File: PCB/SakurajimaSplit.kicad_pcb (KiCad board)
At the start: 2 copper layers, 302 x 112.4 mm, 180 parts, among them J1 SWD, J2 USB-C to Right-Half, J3 VREF+, J4 SWD, J5 USB-C to Host, J6 VREF+, J7 USB-C to Right-Half, SW1 SWCLK/BOOT0, SW2 SWCLK/BOOT0, U1 USBLC6-2SC6, U10 ZJY_M233, U11 ZJY_M233, U2 STM32G0B1CBT6, U3 W25Q128JVS, U4 TLV76733DRVR, U5 USBLC6-2SC6, U6 STM32G0B1CBT6, U7 W25Q128JVS, U8 TLV76733DRVR, U9 USBLC6-2SC6, Y1 8MHz, Y2 8MHz

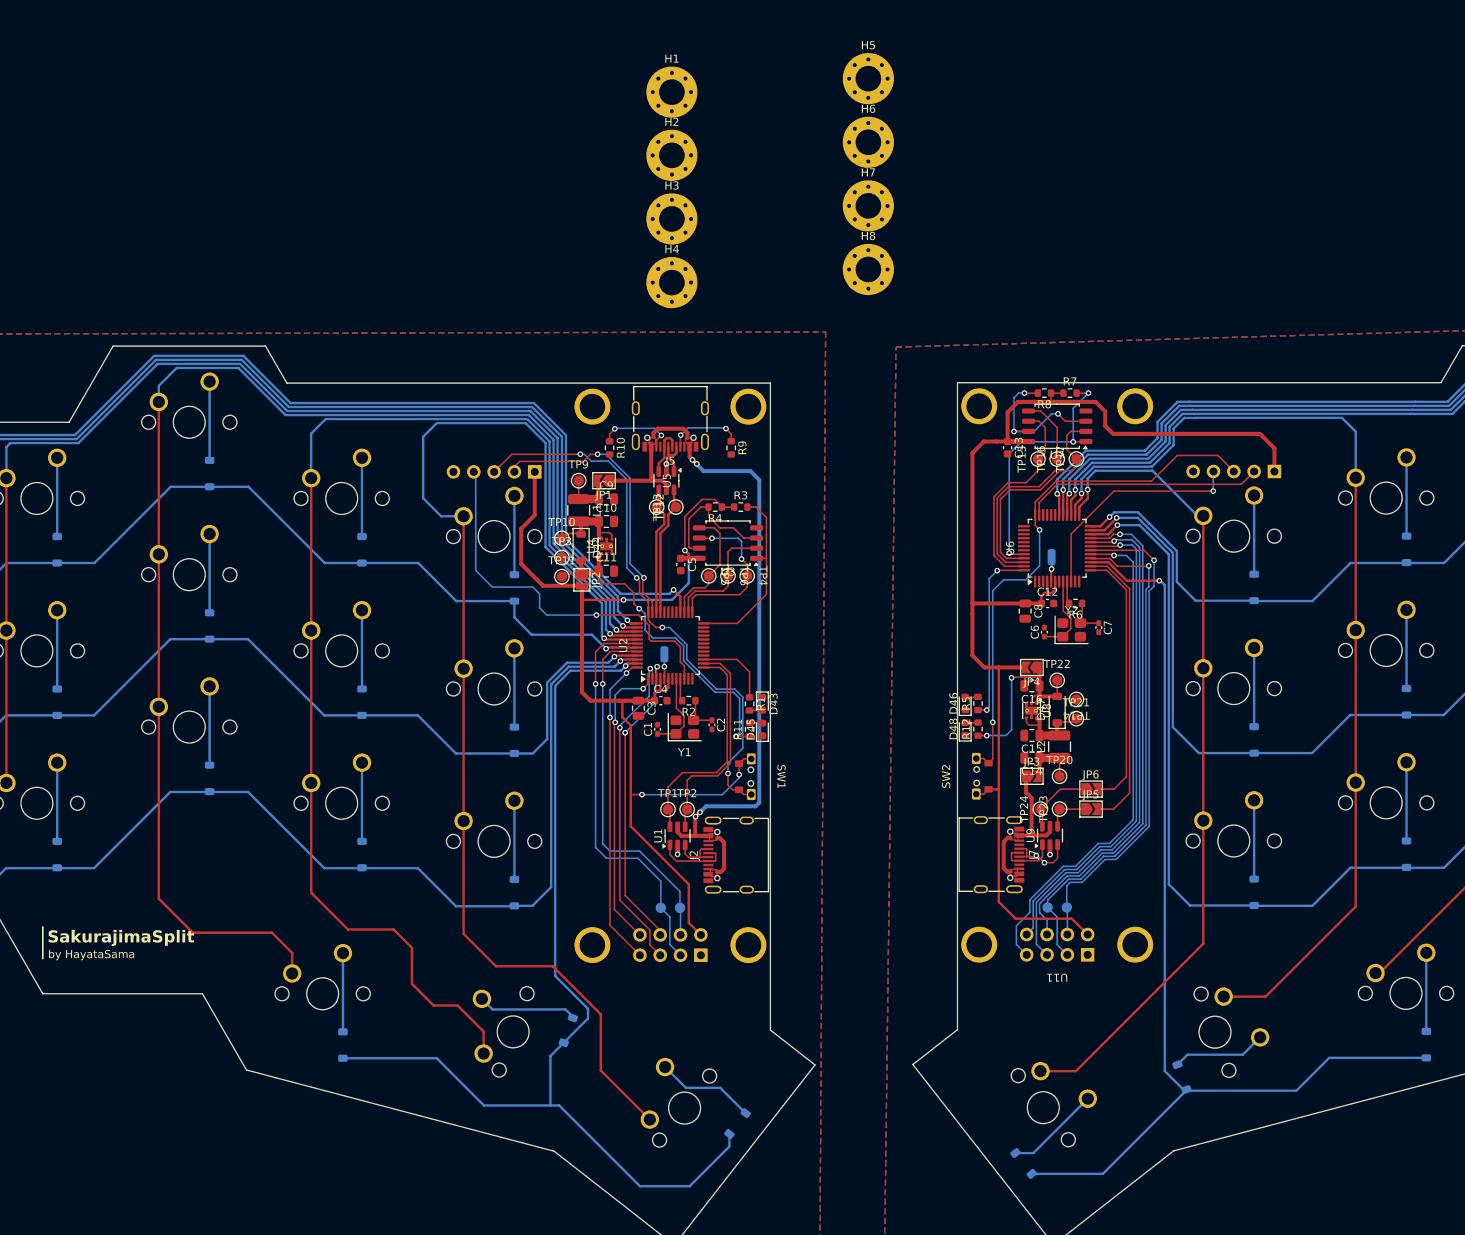
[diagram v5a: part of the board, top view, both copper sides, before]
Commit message: fix(pcb): fix DRC errors, fix silkscreen, fix some routing
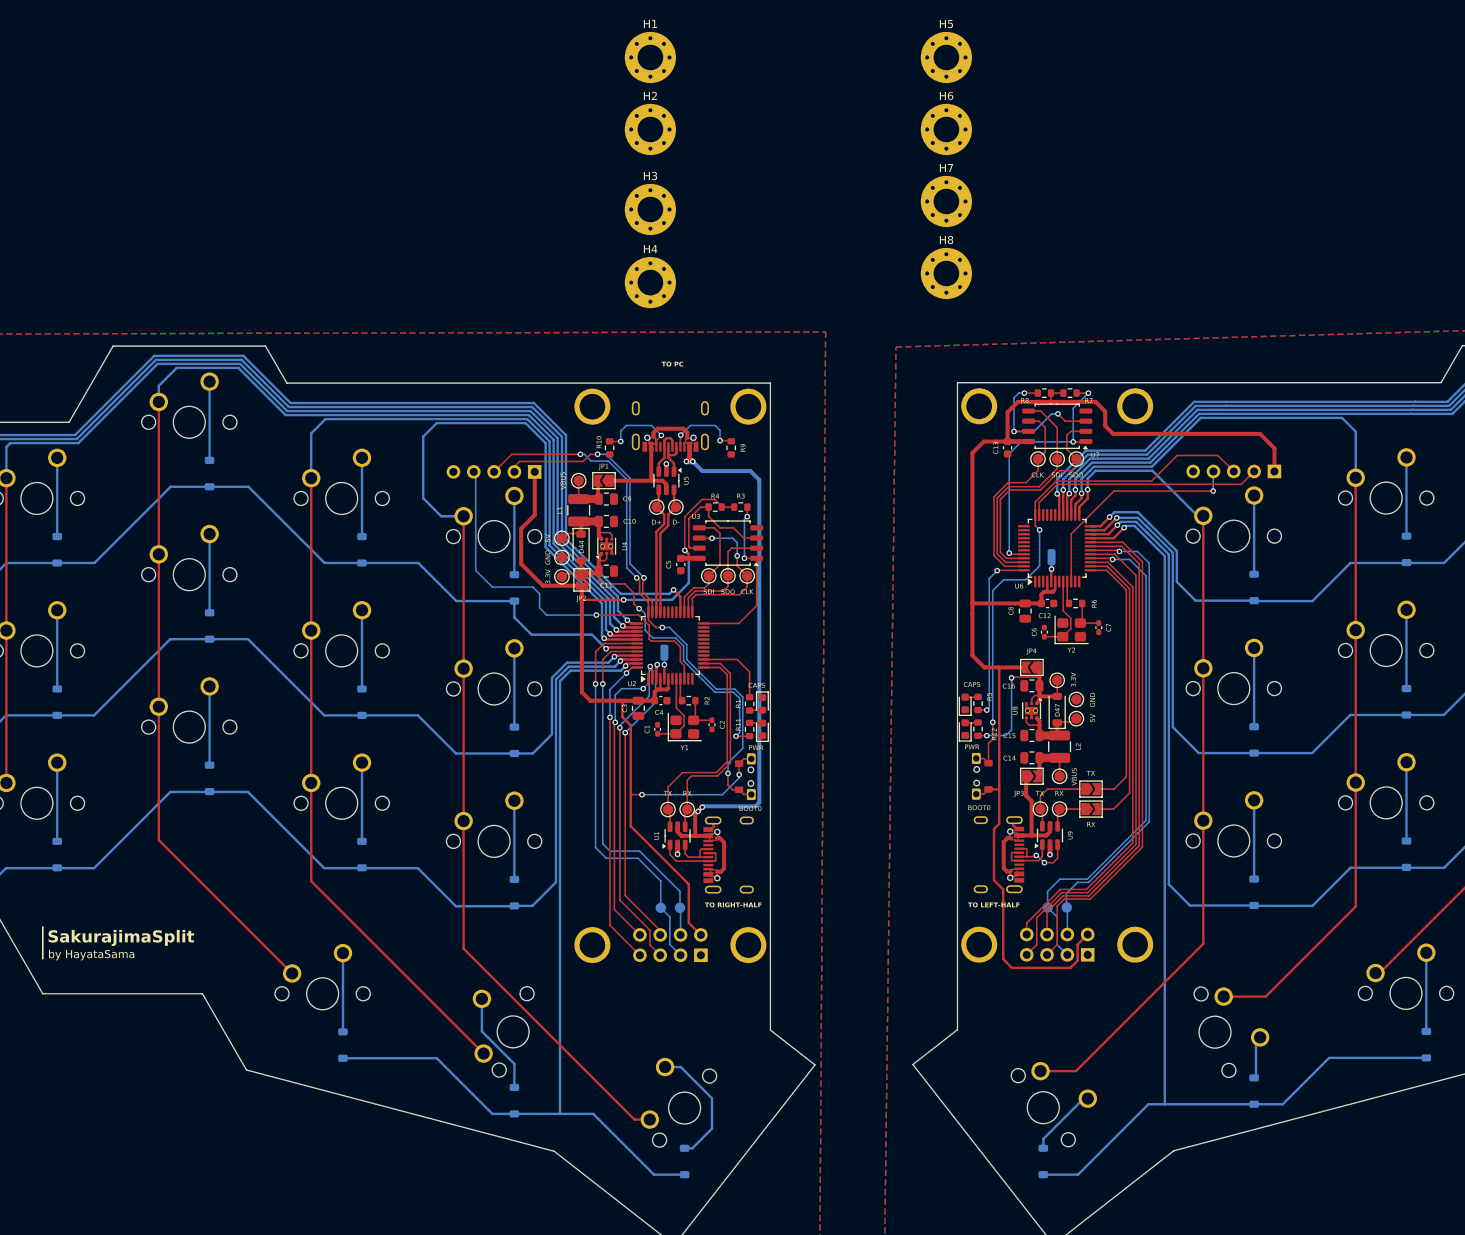
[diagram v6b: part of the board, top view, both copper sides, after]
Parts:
- moved D20 11.1 mm to (147.0, 186.4), turned to 90 degrees
- moved H5 10.1 mm to (201.0, 56.0)
- moved H6 9.89 mm to (201.0, 65.0)
- moved H7 9.77 mm to (201.0, 74.0)
- moved H8 9.77 mm to (201.0, 83.0)
- moved D41 9.18 mm to (239.5, 185.2), turned to 90 degrees
- moved D21 8.13 mm to (168.3, 194.0), turned to 90 degrees
- moved H1 5.10 mm to (164.0, 56.0)
- moved H2 4.21 mm to (164.0, 65.0)
- moved H3 2.94 mm to (164.0, 75.0)
- moved H4 2.69 mm to (164.0, 84.1)
- moved D40 2.48 mm to (213.1, 194.0), turned to 90 degrees
- moved VREF 0.20 mm to (165.8, 130.4)
- renumbered TP22 to 3.3V, TP11 to 3.3V, TP21 to 5V, TP10 to 5V, SW2 to BOOT0, SW1 to BOOT0, D43 to CAPS, D46 to CAPS, TP15 to CLK, TP4 to CLK, TP18 to CLK, TP7 to CLK, TP13 to D+, TP12 to D-, TP14 to GND, TP3 to GND, D48 to PWR, D45 to PWR, TP2 to RX, TP23 to RX, JP5 to RX, TP5 to SDI, TP16 to SDI, TP19 to SDI, TP8 to SDI, TP6 to SDO, TP17 to SDO, JP6 to TX, TP24 to TX, TP1 to TX, TP9 to VBUS, TP20 to VBUS, J3 to VREF, J6 to VREF
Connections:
- U6 pad 15: /Right-Half/ROW3 -> /Right-Half/Display_~{EN}
- U6 pad 19: /Right-Half/Display_~{EN} -> /Right-Half/Display_DC
- U6 pad 21: /Right-Half/Display_DC -> /Right-Half/ROW3
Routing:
- net /Left-Half/ROW3: track 126.1 -> 113.4 mm
- net +3.3V: track 280.9 -> 290.0 mm
- net Net-(D41-A): track 11.7 -> 5.37 mm
- net /Left-Half/COL3: track 169.8 -> 164.0 mm
- net /Left-Half/COL4: track 153.9 -> 148.8 mm
- net /Right-Half/Display_~{EN}: track 61.6 -> 57.4 mm, vias 1 -> 0
- net GND: track 7.03 -> 10.8 mm
- net /Right-Half/ROW3: track 130.4 -> 134.0 mm
- net /Right-Half/Display_DC: track 63.4 -> 60.0 mm, vias 1 -> 0
- net Net-(D21-A): track 12.5 -> 15.7 mm
- net Net-(D40-A): track 12.2 -> 9.19 mm
- net /Left-Half/COL5: track 151.5 -> 148.5 mm
- net /Right-Half/Display_SDI: track 61.5 -> 59.6 mm
- net /Right-Half/Display_~{RST}: track 65.2 -> 63.5 mm, vias 1 -> 0
- net /Left-Half/Flash_~{CS}: track 23.1 -> 21.6 mm, vias 0 -> 2
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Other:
- board text added: "3.3V"
- board text added: "GND"
- board text added: "NRST"
- board text added: "SWCLK"
- board text added: "SWDIO"
- board text added: "TO LEFT-HALF"
- board text added: "TO PC"
- board text added: "TO RIGHT-HALF"

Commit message: feat(pcb): add mounting holes, fix some bugs
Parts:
- added H10: Plate MountingHole, MountingHole:MountingHole_2.2mm_M2_Pad_Via, B.Cu at (162.1, 175.1)
- added H11: Case MountingHole, MountingHole:MountingHole_3.2mm_M3_Pad_Via, B.Cu at (322.6, 125.4)
- added H12: Case MountingHole, MountingHole:MountingHole_3.2mm_M3_Pad_Via, B.Cu at (322.6, 144.4)
- added H13: Case MountingHole, MountingHole:MountingHole_3.2mm_M3_Pad_Via, B.Cu at (246.9, 120.6)
- added H14: Case MountingHole, MountingHole:MountingHole_3.2mm_M3_Pad_Via, B.Cu at (246.9, 163.5)
- added H15: Plate MountingHole, MountingHole:MountingHole_2.2mm_M2_Pad_Via, B.Cu at (304.1, 125.4)
- added H16: Plate MountingHole, MountingHole:MountingHole_2.2mm_M2_Pad_Via, B.Cu at (304.1, 144.4)
- added H17: Plate MountingHole, MountingHole:MountingHole_2.2mm_M2_Pad_Via, B.Cu at (266.0, 111.1)
- added H18: Plate MountingHole, MountingHole:MountingHole_2.2mm_M2_Pad_Via, B.Cu at (266.0, 158.7)
- added H19: Plate MountingHole, MountingHole:MountingHole_2.2mm_M2_Pad_Via, B.Cu at (246.9, 139.7)
- added H20: Plate MountingHole, MountingHole:MountingHole_2.2mm_M2_Pad_Via, B.Cu at (219.4, 175.1)
- added H9: Plate MountingHole, MountingHole:MountingHole_2.2mm_M2_Pad_Via, B.Cu at (134.4, 139.7)
- H1, H2, H3, H4: value MountingHole -> Case MountingHole; moved to B.Cu
- H5, H6, H7, H8: value MountingHole -> Plate MountingHole; footprint MountingHole:MountingHole_3.2mm_M3_Pad_Via -> MountingHole:MountingHole_2.2mm_M2_Pad_Via; moved to B.Cu
- J7: value USB-C to Right-Half -> USB-C to Left-Half
- moved H6 147.0 mm to (77.3, 144.5), turned to 180 degrees
- moved H5 138.7 mm to (78.3, 120.7), turned to 180 degrees
- moved H2 131.9 mm to (58.7, 144.5), turned to 180 degrees
- moved H1 126.1 mm to (58.7, 125.4), turned to 180 degrees
- moved H8 114.3 mm to (115.4, 158.8), turned to 180 degrees
- moved H7 93.3 mm to (115.4, 111.1), turned to 180 degrees
- moved H4 84.7 mm to (134.4, 163.5), turned to 180 degrees
- moved H3 54.3 mm to (134.7, 120.7), turned to 180 degrees
- moved D38 1.05 mm to (315.7, 159.3)
- moved D39 1.05 mm to (334.7, 159.3)
- moved D14 1.00 mm to (70.8, 159.4)
- moved D13 1.00 mm to (51.8, 159.4)
- turned D46 to -90 degrees
- turned R5 to -90 degrees
- renumbered CAPS to D43, PWR to D45, CAPS to D46, PWR to D48, VREF to J3, VREF to J6, RX to JP5, TX to JP6, BOOT0 to SW1, BOOT0 to SW2, TX to TP1, 5V to TP10, 3.3V to TP11, D- to TP12, D+ to TP13, GND to TP14, CLK to TP15, SDI to TP16, SDO to TP17, CLK to TP18, SDI to TP19, RX to TP2, VBUS to TP20, 5V to TP21, 3.3V to TP22, RX to TP23, TX to TP24, GND to TP3, CLK to TP4, SDI to TP5, SDO to TP6, CLK to TP7, SDI to TP8, VBUS to TP9
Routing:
- net /Left-Half/ROW0: track 126.2 -> 129.6 mm
- net /Right-Half/COL1: track 123.5 -> 120.4 mm
- net /Right-Half/ROW0: track 135.1 -> 137.8 mm
- net /Left-Half/ROW1: track 131.6 -> 133.9 mm
- net /Right-Half/ROW1: track 153.1 -> 155.4 mm
- net /Right-Half/CapsLock: track 22.4 -> 20.8 mm
- net Net-(D39-A): track 9.84 -> 8.79 mm
- net Net-(D38-A): track 9.84 -> 8.79 mm
- net Net-(D13-A): track 9.84 -> 8.84 mm
- net Net-(D14-A): track 9.84 -> 8.84 mm
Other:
- board size 302 x 112.4 mm -> 302 x 112 mm
- board text added: "5V"
- board text added: "BOOT0"
- board text added: "CAPS"
- board text added: "CLK"
- board text added: "D+"
- board text added: "D-"
- board text added: "PWR"
- board text added: "RX"
- board text added: "SDI"
- board text added: "SDO"
- board text added: "TX"
- board text added: "VBUS"
- board text added: "VREF"
